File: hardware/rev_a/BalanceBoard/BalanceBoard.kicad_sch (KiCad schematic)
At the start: 54 parts, among them J1 48037-0001, J2 5103309-1, J3 2212S-04SG-85, T00 TestPoints, T01 TestPoints, T02 TestPoints, T03 TestPoints, T04 TestPoints, T05 TestPoints, T06 TestPoints, T07 TestPoints, T10 TestPoints, T11 TestPoints, T12 TestPoints, T13 TestPoints, T14 TestPoints, T15 TestPoints, T16 TestPoints, T17 TestPoints, T21 TestPoints, T31 TestPoints, T32 TestPoints, T33 TestPoints, T40 TestPoints, T41 TestPoints, T42 TestPoints, T43 TestPoints, T44 TestPoints, T45 TestPoints, T46 TestPoints, T47 TestPoints, T48 TestPoints, T49 TestPoints, T50 TestPoints, U1 C8051F850-A-GU, U2 FT232RL

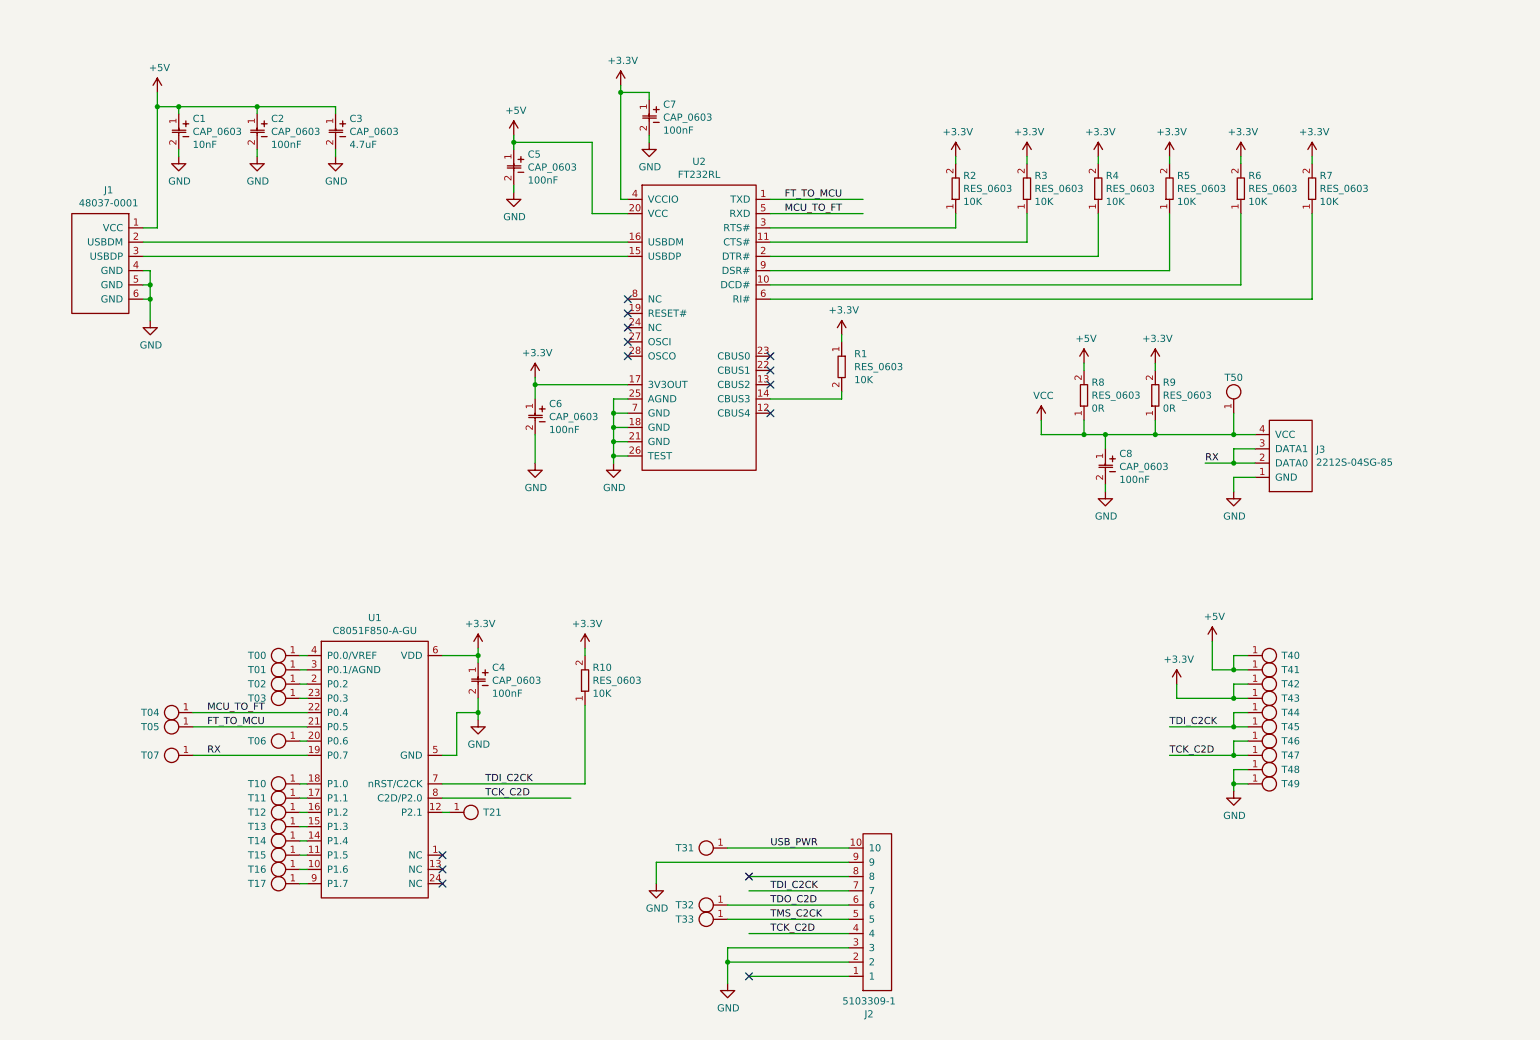
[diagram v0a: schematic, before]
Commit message: change usb
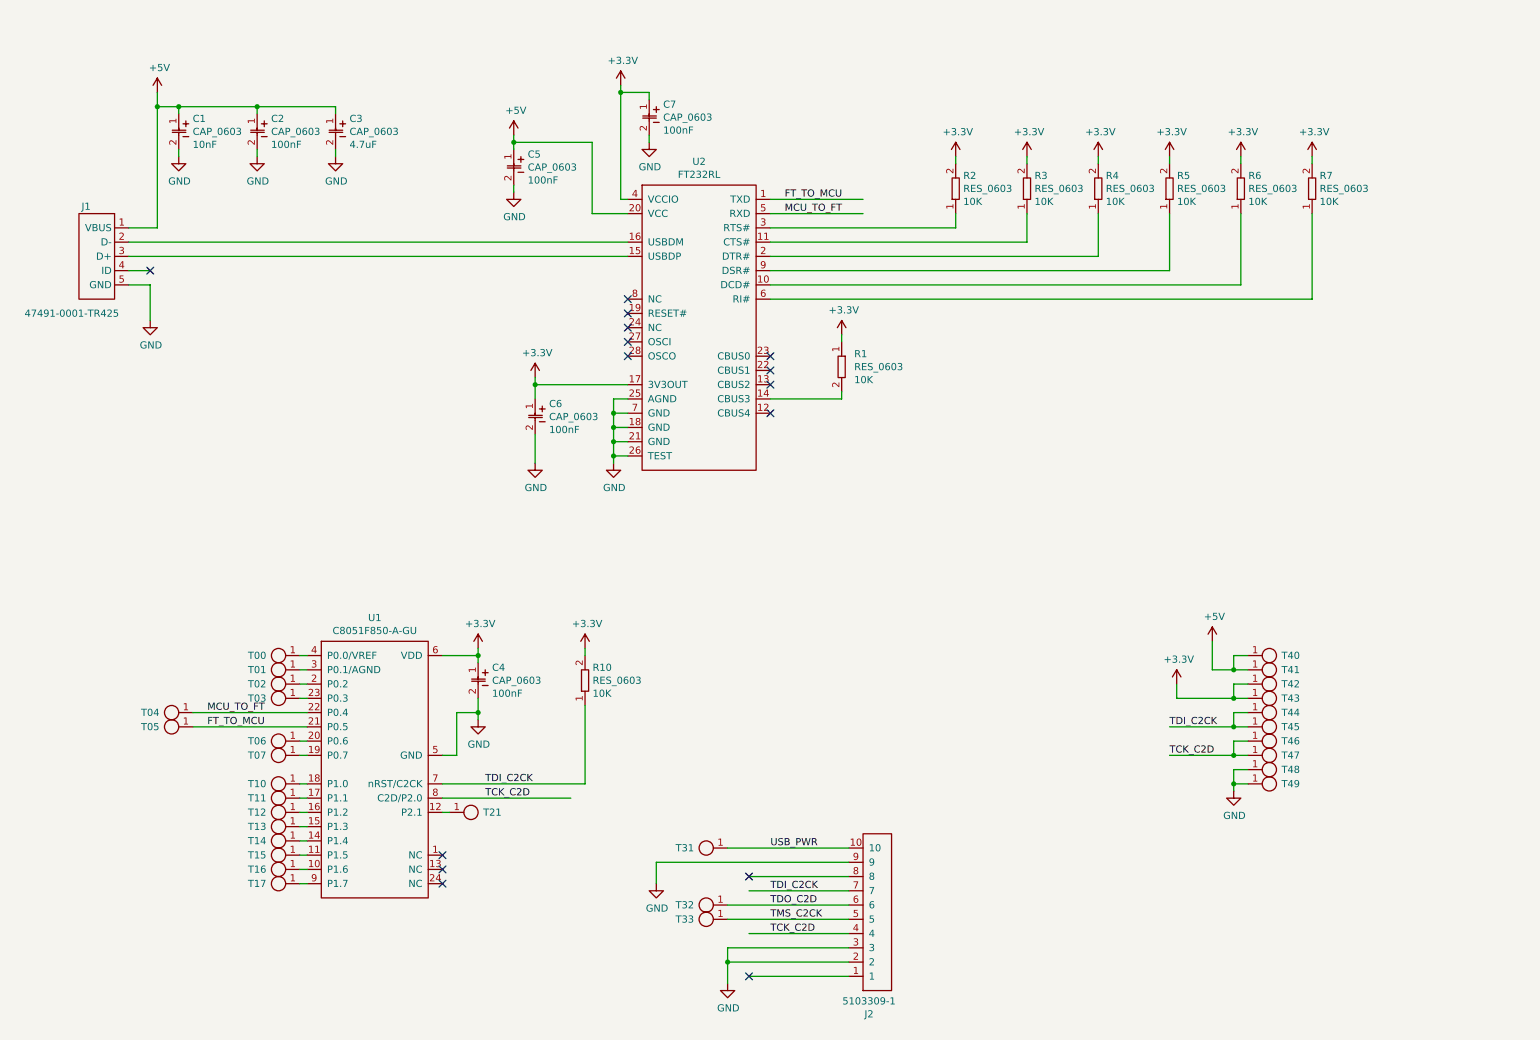
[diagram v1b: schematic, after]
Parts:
- removed C8: CAP_0603, receiver:0603, symbol BalanceBoard-rescue:CAP_0603-receiver
- removed J1: 48037-0001, receiver:48037-0001, symbol BalanceBoard-rescue:48037-0001-receiver
- removed J3: 2212S-04SG-85, receiver:2212S-04SG-85, symbol BalanceBoard-rescue:2212S-04SG-85-receiver
- removed R8, R9: RES_0603, receiver:0603, symbol BalanceBoard-rescue:RES_0603-receiver
- removed T50: TestPoints, receiver:TestPoint, symbol BalanceBoard-rescue:TestPoints-receiver
- added J1: 47491-0001-TR425, receiver:47491-0001-TR425, symbol BalanceBoard:47491-0001-TR425
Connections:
- net +5V: now also J1.1 (VBUS)
- net GND: now also J1.5 (GND)
- net at U2.15 (USBDP): now also J1.3 (D+)
- net at U2.16 (USBDM): now also J1.2 (D-)
- net RX: no longer names the net of T07.1, U1.19 (P0.7)
- no-connect marks 14 -> 15
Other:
- moved on the sheet: T07

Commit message: rev a fab out
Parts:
- added C10, C11, C13, C3, C5, C9: CAP_0603, receiver:0603, symbol BalanceBoard-rescue:CAP_0603-receiver
- added R1, R10, R12, R13, R14, R15, R16, R17, R18, R19, R2, R20, R22, R23, R8: RES_0603, receiver:0603, symbol BalanceBoard-rescue:RES_0603-receiver
- added T1, T10, T11, T12, T13, T16, T17, T19, T20, T22, T23, T43, T44, T45, T48, T7, T8, T9: TestPoints, receiver:TestPoint, symbol BalanceBoard-rescue:TestPoints-receiver
- added U1: MPU-6050, Sensor_Motion:InvenSense_QFN-24_4x4mm_P0.5mm, symbol Sensor_Motion:MPU-6050
- added U4: DRV2605LDGST, receiver:DRV2605LDGST, symbol BalanceBoard:DRV2605LDGST
- renumbered C4 to C12, C3 to C4, C7 to C6, C5 to C7, C6 to C8, R7 to R11, R10 to R21, R2 to R3, R3 to R4, R1 to R5, R4 to R6, R5 to R7, R6 to R9, T40 to T14, T41 to T15, T42 to T18, T31 to T2, T43 to T21, T48 to T24, T49 to T25, T04 to T26, T05 to T27, T10 to T28, T13 to T29, T44 to T3, T14 to T30, T16 to T31, T17 to T32, T00 to T33, T01 to T34, T02 to T35, T03 to T36, T06 to T37, T07 to T38, T11 to T39, T32 to T4, T12 to T40, T15 to T41, T21 to T42, T33 to T5, T45 to T6, U1 to U3
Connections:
- net +3V3: now also R5.2, C3.1, C5.1, R1.1, R10.2, R15.2, R18.2, T19.1, T20.1, U1.13 (VDD), U1.8 (VDDIO); no longer R5.1
- net +5V: now also R19.2, R22.2, R8.2, T16.1, T17.1
- net GND: now also C10.2, C11.2, C13.2, C3.2, C5.2, C9.2, R2.2, T22.1, T23.1, U1.1 (CLKIN), U1.11 (FSYNC), U1.18 (GND), U4.8 (GND)
- net TCK_C2D: now also T6.1; no longer T46.1, T47.1
- net TDI_C2CK: no longer T6.1
- net SDA: now reaches T31.1, U3.10 (P1.6)
- net SDA: now also R16.1, R18.1, R19.1, R20.1
- net TRIG: now reaches T30.1, U3.14 (P1.4)
- net TRIG: now also R14.1
- net EN: now reaches T29.1, U3.15 (P1.3)
- net EN: now also R13.1
- net INT: now reaches T28.1, U3.18 (P1.0)
- net INT: now also R12.1
- net SCL: now reaches T32.1, U3.9 (P1.7)
- net SCL: now also R15.1, R17.1, R22.1, R23.1
- net at U2.14 (CBUS3): now also R5.1; no longer R5.2
- net D+: now reaches J1.3 (D+), U2.15 (USBDP)
- net D-: now reaches J1.2 (D-), U2.16 (USBDM)
- net at J1.4 (ID): now also T1.1
- new net: C11.1, U4.1 (REG)
- new net: C9.1, U1.10 (REGOUT)
- new net: T8.1, U1.6 (AUX_SDA)
- new net: C10.1, U1.20 (CPOUT)
- new net: T9.1, U1.7 (AUX_SCL)
- new net DRV_EN: R13.2, U4.5 (EN)
- new net DRV_SCL: R17.2, U4.2 (SCL)
- new net DRV_SDA: R16.2, U4.3 (SDA)
- new net DRV_TRIG: R14.2, U4.4 (IN/TRIG)
- new net MPU_AD0: R1.2, R2.1, U1.9 (AD0)
- new net MPU_INT: R12.2, T7.1, U1.12 (INT)
- new net MPU_SCL: R23.2, U1.23 (SCL)
- new net MPU_SDA: R20.2, U1.24 (SDA)
- new net OUT+: T46.1, T47.1, T48.1, U4.7 (OUT+)
- new net OUT-: T43.1, T44.1, T45.1, U4.9 (OUT-)
- new net Vdrive: C13.1, R10.1, R8.1, T10.1, T11.1, T12.1, T13.1, U4.10 (VDD), U4.6 (VDD/NC)
- no-connect marks 15 -> 14
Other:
- note added: "Driver"
- note added: "I2C b1011010 0xB4 (Write) 0xB5 (Read)"
- note added: "I2C b1101000 (AD0 == 0) b1101001 (AD1 == 1) 0xD0 (Write)(AD0 == 0) 0xD1 (Read)(AD0 == 0) 0xD2 (Write)(AD1 == 1) 0xD3 (Read)(AD1 == 1)"
- note added: "MCU"
- note added: "MCU Prog Conn"
- note added: "MPU"
- note added: "Res Config"
- note added: "TestPoints"
- note added: "USB Conn"
- note added: "USB to UART"
- moved on the sheet: C1, C12, C2, C4, C6, C7, C8, R11, R21, R3, R4, R5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
